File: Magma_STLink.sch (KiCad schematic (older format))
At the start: 44 parts

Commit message: PCB
PCB'ye geçildi. Boyutları düzeltilerek PCB'ye devam edilecek.
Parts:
- D7: renamed from D?; footprint SOT95P280X145-6N -> ESDA6V1BC6:SOT95P280X145-6N
- R14: renamed from R?; footprint (none) -> Resistor_SMD:R_0805_2012Metric_Pad1.20x1.40mm_HandSolder
- U1: renamed from U?; footprint (none) -> Package_TO_SOT_SMD:SOT-223-3_TabPin2
- gave numbers to parts that had none: 40
- renumbered STLINK_CONN to STLINK_CONN1
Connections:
- net USB_DM: no longer U2.32 (PA11)
- net USB_DP: no longer U2.33 (PA12)
- new net USB_M: U2.32 (PA11)
- new net USB_P: U2.33 (PA12)
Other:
- moved on the sheet: R13

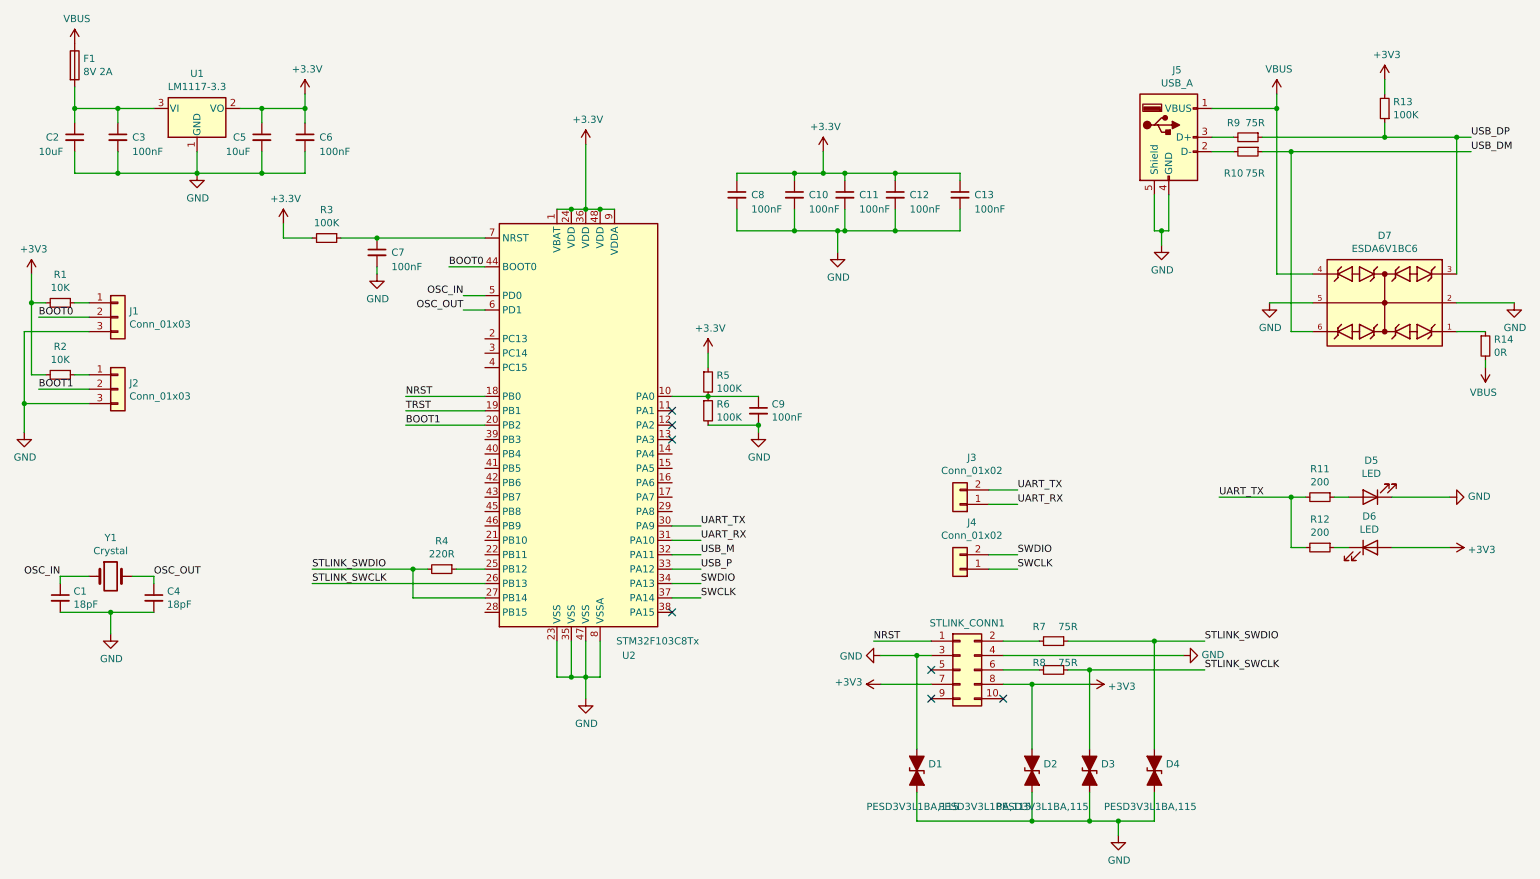
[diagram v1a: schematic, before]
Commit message: PCB tamamlandı * PCB tamamlandı ve şematikte küçük değişiklikler yapıldı. * DRC yapıldı herhangi bir hata çıkmadı.
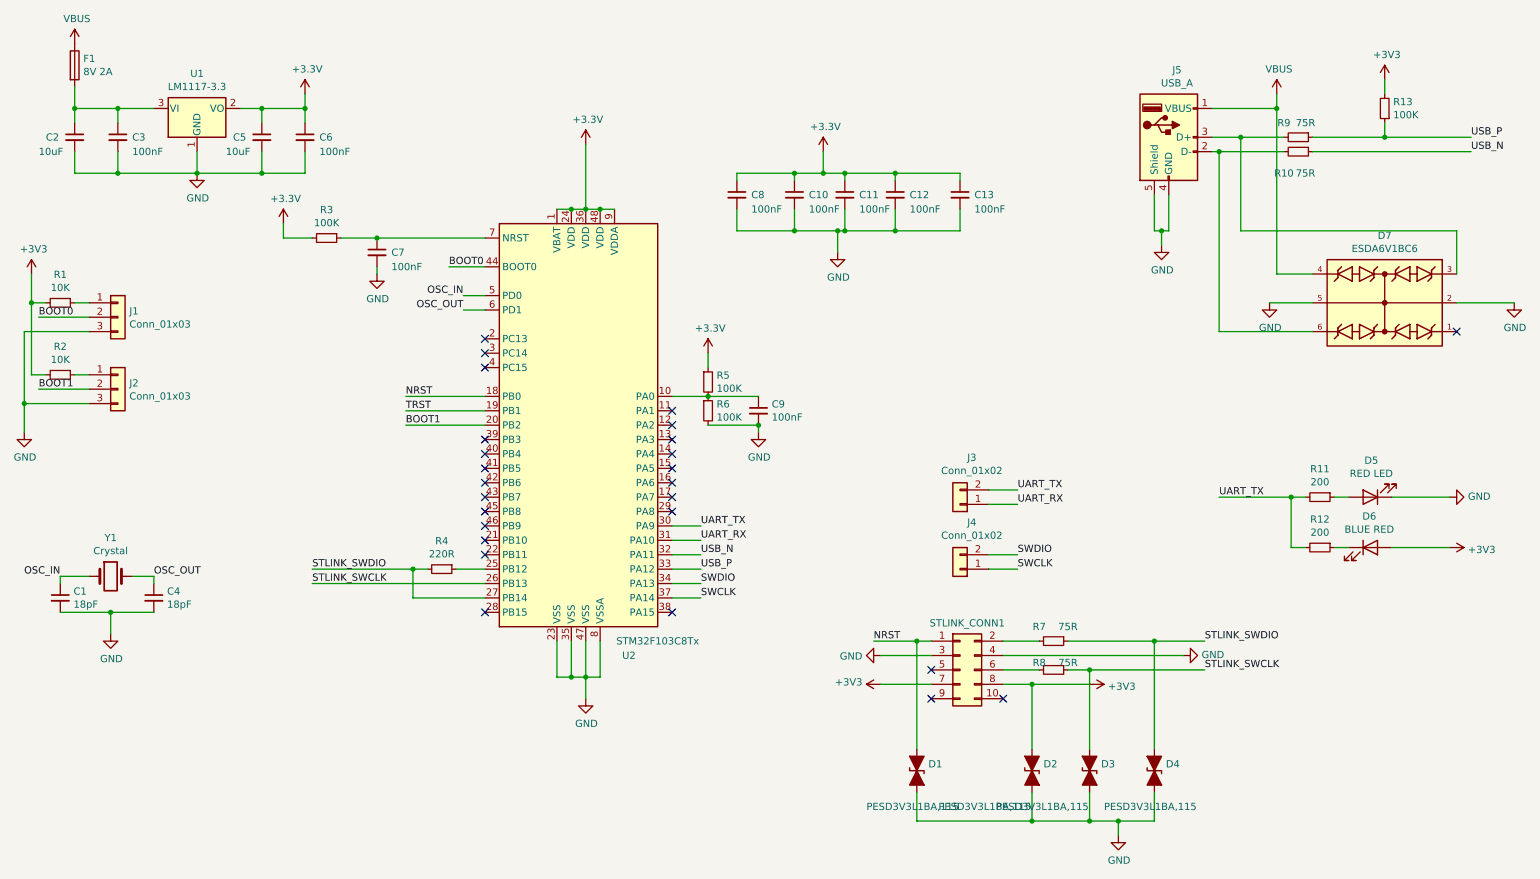
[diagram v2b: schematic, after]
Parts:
- removed R14: 0R, Resistor_SMD:R_0805_2012Metric_Pad1.20x1.40mm_HandSolder, symbol Device:R_Small
- D5: value LED -> RED LED
- D6: value LED -> BLUE RED
- J5: footprint Connector_USB:USB_A_CONNFLY_DS1095-WNR0 -> Connector_USB:USB_A_CNCTech_1001-011-01101_Horizontal; Manufacturer Link https://www.ozdisan.com/konnektor-kablo-baglanti-elemanlari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 -> https://www.ozdisan.com/connectors-and-interconnects/usb-dv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
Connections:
- net USB_M is gone; now on net USB_N: U2.32 (PA11)
- net GND: no longer D1.1 (A1)
- net NRST: now also D1.1 (A1)
- net USB_P: now also R13.1, R9.1
- net at J5.2 (D-), R10.2: now also D7.6
- net at J5.3 (D+), R9.2: now also D7.3
- net USB_DM renamed USB_N
- net USB_N: no longer D7.6
- removed net USB_DP: D7.3, R13.1, R9.1
- no-connect marks 7 -> 26
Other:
- moved on the sheet: R10, R9
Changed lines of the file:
@@
 	5200 4450 5400 4450
 Text Label 5400 4350 0    50   ~ 0
-USB_M
+USB_N
 Text Label 5400 4450 0    50   ~ 0
 USB_P
@@
 F 0 "J5" H 8707 1917 50  0000 C CNN
 F 1 "USB_A" H 8707 1826 50  0000 C CNN
-F 2 "Connector_USB:USB_A_CONNFLY_DS1095-WNR0" H 8800 1400 50  0001 C CNN
+F 2 "Connector_USB:USB_A_CNCTech_1001-011-01101_Horizontal" H 8800 1400 50  0001 C CNN
 F 3 "https://cdn.ozdisan.com/ETicaret_Dosya/348007_2646947.pdf" H 8800 1400 50  0001 C CNN
-F 4 "https://www.ozdisan.com/konnektor-kablo-baglanti-elemanlari/usb-dvi-hdmi-konnektorler/usb-konnektorler/DS1095-WNR0" H 8650 1450 50  0001 C CNN "Manufacturer Link"
+F 4 "https://www.ozdisan.com/connectors-and-interconnects/usb-dvi-hdmi-connectors/usb-connectors/DS1098-WN0" H 8650 1450 50  0001 C CNN "Manufacturer Link"
 	1    8650 1450
 	1    0    0    -1
@@
 L Device:R_Small R9
 U 1 1 614F9BCC
-P 9200 1450
-F 0 "R9" V 9100 1350 50  0000 C CNN
-F 1 "75R" V 9100 1500 50  0000 C CNN
-F 2 "Resistor_SMD:R_0805_2012Metric_Pad1.20x1.40mm_HandSolder" H 9200 1450 50  0001 C CNN
-F 3 "~" H 9200 1450 50  0001 C CNN
-F 4 "https://www.ozdisan.com/passive-components/resistors/smt-smd-and-chip-resistors/0805S8F750JT5E" V 9200 1450 50  0001 C CNN "Manufacturer Link"
-	1    9200 1450
+P 9550 1450
+F 0 "R9" V 9450 1350 50  0000 C CNN
+F 1 "75R" V 9450 1500 50  0000 C CNN
+F 2 "Resistor_SMD:R_0805_2012Metric_Pad1.20x1.40mm_HandSolder" H 9550 1450 50  0001 C CNN
+F 3 "~" H 9550 1450 50  0001 C CNN
+F 4 "https://www.ozdisan.com/passive-components/resistors/smt-smd-and-chip-resistors/0805S8F750JT5E" V 9550 1450 50  0001 C CNN "Manufacturer Link"
+	1    9550 1450
 	0    1    1    0
 $EndComp
@@
 L Device:R_Small R10
 U 1 1 614F9F4A
-P 9200 1550
-F 0 "R10" V 9350 1450 50  0000 C CNN
-F 1 "75R" V 9350 1600 50  0000 C CNN
-F 2 "Resistor_SMD:R_0805_2012Metric_Pad1.20x1.40mm_HandSolder" H 9200 1550 50  0001 C CNN
-F 3 "~" H 9200 1550 50  0001 C CNN
-F 4 "https://www.ozdisan.com/passive-components/resistors/smt-smd-and-chip-resistors/0805S8F750JT5E" V 9200 1550 50  0001 C CNN "Manufacturer Link"
-	1    9200 1550
-	0    1    1    0
-$EndComp
-Wire Wire Line
-	8950 1450 9100 1450
-Wire Wire Line
-	9100 1550 8950 1550
+P 9550 1550
+F 0 "R10" V 9700 1450 50  0000 C CNN
+F 1 "75R" V 9700 1600 50  0000 C CNN
+F 2 "Resistor_SMD:R_0805_2012Metric_Pad1.20x1.40mm_HandSolder" H 9550 1550 50  0001 C CNN
+F 3 "~" H 9550 1550 50  0001 C CNN
+F 4 "https://www.ozdisan.com/passive-components/resistors/smt-smd-and-chip-resistors/0805S8F750JT5E" V 9550 1550 50  0001 C CNN "Manufacturer Link"
+	1    9550 1550
+	0    1    1    0
+$EndComp
+Wire Wire Line
+	8950 1450 9150 1450
+Wire Wire Line
+	9450 1550 9000 1550
 $Comp
 L Device:C_Small C7
@@
 NoConn ~ 5200 3450
 NoConn ~ 5200 3550
-Wire Wire Line
-	9300 1550 9500 1550
 Text Label 10750 1550 0    50   ~ 0
-USB_DM
+USB_N
 Text Label 10750 1450 0    50   ~ 0
-USB_DP
+USB_P
 $Comp
 L Device:R_Small R4
@@
 P 10050 3950
 F 0 "D5" H 10043 3695 50  0000 C CNN
-F 1 "LED" H 10043 3786 50  0000 C CNN
+F 1 "RED LED" H 10043 3786 50  0000 C CNN
 F 2 "LED_SMD:LED_0603_1608Metric_Pad1.05x0.95mm_HandSolder" H 10050 3950 50  0001 C CNN
 F 3 "~" H 10050 3950 50  0001 C CNN
@@
 P 10050 4300
 F 0 "D6" H 10043 4517 50  0000 C CNN
-F 1 "LED" H 10043 4426 50  0000 C CNN
+F 1 "BLUE RED" H 10043 4426 50  0000 C CNN
 F 2 "LED_SMD:LED_0603_1608Metric_Pad1.05x0.95mm_HandSolder" H 10050 4300 50  0001 C CNN
 F 3 "~" H 10050 4300 50  0001 C CNN
@@
 NRST
 Wire Wire Line
-	6600 4950 7000 4950
+	6600 4950 6900 4950
 $Comp
 L power:GND #PWR0119
@@
 Wire Wire Line
 	6650 5250 7000 5250
-Wire Wire Line
-	6650 5050 6900 5050
 $Comp
 L power:+3V3 #PWR0121
@@
 	9650 2400 9400 2400
 Wire Wire Line
-	9650 2800 9500 2800
-Wire Wire Line
-	9500 2800 9500 1550
-Connection ~ 9500 1550
-Wire Wire Line
-	9500 1550 10750 1550
-Wire Wire Line
 	9400 1150 9400 1250
 Wire Wire Line
@@
 Wire Wire Line
 	9400 1250 9400 2400
-Connection ~ 10650 1450
-Wire Wire Line
-	10650 1450 10750 1450
-Wire Wire Line
-	10650 1450 10650 2400
 $Comp
 L Device:D_TVS_ALT D3
@@
 Wire Wire Line
 	8300 6200 8550 6200
-$Comp
-L power:VBUS #PWR0126
-U 1 1 6164474E
-P 10850 3050
-F 0 "#PWR0126" H 10850 2900 50  0001 C CNN
-F 1 "VBUS" H 10865 3223 50  0000 C CNN
-F 2 "" H 10850 3050 50  0001 C CNN
-F 3 "" H 10850 3050 50  0001 C CNN
-	1    10850 3050
-	-1   0    0    1
-$EndComp
-$Comp
-L Device:R_Small R14
-U 1 1 6164B2BE
-P 10850 2900
-F 0 "R14" H 10909 2946 50  0000 L CNN
-F 1 "0R" H 10909 2855 50  0000 L CNN
-F 2 "Resistor_SMD:R_0805_2012Metric_Pad1.20x1.40mm_HandSolder" H 10850 2900 50  0001 C CNN
-F 3 "~" H 10850 2900 50  0001 C CNN
-	1    10850 2900
-	1    0    0    -1
-$EndComp
-Wire Wire Line
-	10850 2800 10650 2800
-Wire Wire Line
-	10850 3000 10850 3050
 $Comp
 L Connector_Generic:Conn_02x05_Odd_Even STLINK_CONN1
@@
 $EndComp
 Wire Wire Line
-	6900 5050 6900 5700
-Connection ~ 6900 5050
-Wire Wire Line
-	6900 5050 7000 5050
-Wire Wire Line
 	6900 6000 6900 6200
 Wire Wire Line
@@
 	10150 1050 10150 1150
 Wire Wire Line
-	9300 1450 10150 1450
+	9650 1450 10150 1450
 Wire Wire Line
 	10150 1350 10150 1450
 Connection ~ 10150 1450
-Wire Wire Line
-	10150 1450 10650 1450
+NoConn ~ 3900 4350
+NoConn ~ 3900 4250
+NoConn ~ 3900 4150
+NoConn ~ 3900 4050
+NoConn ~ 3900 3950
+NoConn ~ 3900 3850
+NoConn ~ 3900 3750
+NoConn ~ 3900 3650
+NoConn ~ 3900 3550
+NoConn ~ 3900 3050
+NoConn ~ 3900 2950
+NoConn ~ 5200 3650
+NoConn ~ 5200 3750
+NoConn ~ 5200 3850
+NoConn ~ 5200 3950
+NoConn ~ 5200 4050
+NoConn ~ 3900 4750
+NoConn ~ 3900 2850
+Wire Wire Line
+	6650 5050 7000 5050
+Wire Wire Line
+	6900 5700 6900 4950
+Connection ~ 6900 4950
+Wire Wire Line
+	6900 4950 7000 4950
+Wire Wire Line
+	9650 1550 10750 1550
+Wire Wire Line
+	9000 2800 9000 1550
+Wire Wire Line
+	9000 2800 9650 2800
+Connection ~ 9000 1550
+Wire Wire Line
+	9000 1550 8950 1550
+Wire Wire Line
+	10150 1450 10750 1450
+Wire Wire Line
+	10650 2400 10650 2100
+Wire Wire Line
+	10650 2100 9150 2100
+Wire Wire Line
+	9150 2100 9150 1450
+Connection ~ 9150 1450
+Wire Wire Line
+	9150 1450 9450 1450
+NoConn ~ 10650 2800
 $EndSCHEMATC

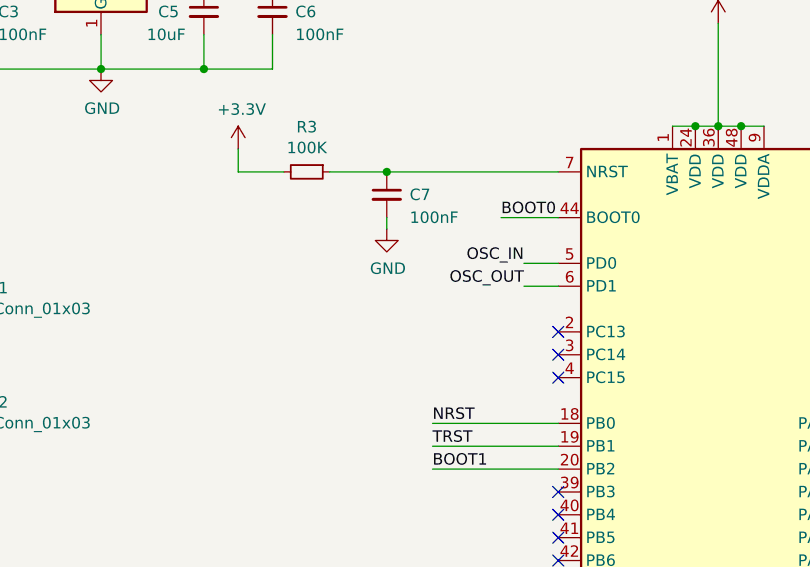
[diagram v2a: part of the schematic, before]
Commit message: Reset'e bir direnç eklendi. Anlık resetleyebilmek için 0805 kılıfında bir direnç eklendi.
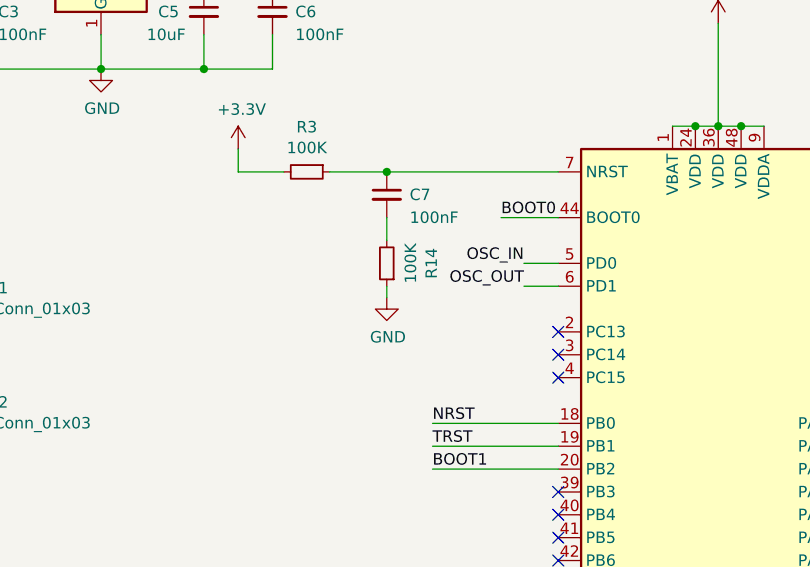
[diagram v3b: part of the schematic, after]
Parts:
- added R14: 100K, Resistor_SMD:R_0805_2012Metric_Pad1.20x1.40mm_HandSolder, symbol Device:R_Small
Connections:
- net GND: now also R14.1; no longer C7.2
- new net: C7.2, R14.2
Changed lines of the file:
@@
 L power:GND #PWR0113
 U 1 1 61540056
-P 3150 2400
-F 0 "#PWR0113" H 3150 2150 50  0001 C CNN
-F 1 "GND" H 3155 2227 50  0000 C CNN
-F 2 "" H 3150 2400 50  0001 C CNN
-F 3 "" H 3150 2400 50  0001 C CNN
-	1    3150 2400
-	1    0    0    -1
-$EndComp
-Wire Wire Line
-	3150 2400 3150 2350
+P 3150 2700
+F 0 "#PWR0113" H 3150 2450 50  0001 C CNN
+F 1 "GND" H 3155 2527 50  0000 C CNN
+F 2 "" H 3150 2700 50  0001 C CNN
+F 3 "" H 3150 2700 50  0001 C CNN
+	1    3150 2700
+	1    0    0    -1
+$EndComp
 Wire Wire Line
 	3900 2350 3650 2350
@@
 	9150 1450 9450 1450
 NoConn ~ 10650 2800
+$Comp
+L Device:R_Small R14
+U 1 1 61697A55
+P 3150 2550
+F 0 "R14" V 2954 2550 50  0000 C CNN
+F 1 "100K" V 3045 2550 50  0000 C CNN
+F 2 "Resistor_SMD:R_0805_2012Metric_Pad1.20x1.40mm_HandSolder" H 3150 2550 50  0001 C CNN
+F 3 "" H 3150 2550 50  0001 C CNN
+	1    3150 2550
+	-1   0    0    1
+$EndComp
+Wire Wire Line
+	3150 2700 3150 2650
+Wire Wire Line
+	3150 2350 3150 2450
 $EndSCHEMATC
